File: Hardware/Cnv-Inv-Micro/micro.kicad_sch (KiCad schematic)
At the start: 48 parts, among them J1 Conn_01x03, SW1 SW_MEC_5E, U1 TMA-1205S-2WR2, U2 TMA-1205S-2WR2, U3 AMS1117-3.3, U4 STM32F103C8Tx, U5 TMA-12012S-2WR3, Y1 Crystal 8MHz

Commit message: Normalizacion placa micros
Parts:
- removed BT1: Battery_Cell, Battery:BatteryHolder_Keystone_1058_1x2032, symbol Device:Battery_Cell
- removed C15, C16: 4.7uF, Capacitor_SMD:CP_Elec_4x5.4, symbol Device:C_Polarized_Small
- removed Cnv_Control_A1: Conn_01x05, Connector_Molex:Molex_KK-254_AE-6410-05A_1x05_P2.54mm_Vertical, symbol Connector_Generic:Conn_01x05
- removed D8, D9: 1N5819WS, Diode_SMD:D_SOD-323_HandSoldering, symbol Diode:1N5819WS
- removed Inv_Pwr_A1: Conn_01x02, Connector_Molex:Molex_KK-254_AE-6410-02A_1x02_P2.54mm_Vertical, symbol Connector_Generic:Conn_01x02
- removed U5: TMA-12012S-2WR3, Converter_DCDC:Converter_DCDC_TRACO_TMA-05xxS_12xxS_Single_THT, symbol Converter_DCDC:TMA-1205S
- added Cooler, TermoSwitch: Conn_01x02, Connector_Molex:Molex_KK-254_AE-6410-02A_1x02_P2.54mm_Vertical, symbol Connector_Generic:Conn_01x02
- added Emg_Button2: Screw_Terminal_01x02, TerminalBlock_Phoenix:TerminalBlock_Phoenix_MKDS-1,5-2_1x02_P5.00mm_Horizontal, symbol Connector:Screw_Terminal_01x02
- added J3: Screw_Terminal_01x07, TerminalBlock_Phoenix:TerminalBlock_Phoenix_PT-1,5-7-5.0-H_1x07_P5.00mm_Horizontal, symbol Connector:Screw_Terminal_01x07
- added R67: 4.7k, Resistor_SMD:R_0603_1608Metric_Pad0.98x0.95mm_HandSolder, symbol Device:R
- added R68: 3.3k, Resistor_SMD:R_0603_1608Metric_Pad0.98x0.95mm_HandSolder, symbol Device:R
- added U24: PC817, Package_DIP:DIP-4_W7.62mm_SMDSocket_SmallPads, symbol Isolator:PC817
- U1: value TMA-1205S-2WR2 -> B1212S-2WR3
- U2: value TMA-1205S-2WR2 -> B1205S-2WR2
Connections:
- net 12V_Cnv: now also Cooler.1 (Pin_1)
- net 3V3_Micro: now also U24.4
- net GND_Micro: now also R68.1
- net Gnd_Cnv: now also Cooler.2 (Pin_2)
- net TermoSw_Input: now also R68.2, U24.3
- new net: TermoSwitch.2 (Pin_2), U24.1
- new net: R67.2, TermoSwitch.1 (Pin_1)
- new net 12V: R67.1
- new net Gnd_NoInsulated: U24.2
- new net Out_Emg1: Emg_Button2.2 (Pin_2)
- new net Out_Emg2: Emg_Button2.1 (Pin_1)
- new net Out_Rpm: J3.1 (Pin_1)
- new net Out_Start: J3.7 (Pin_7)
- new net Out_Stop: J3.6 (Pin_6)
- new net Out_Vel1: J3.5 (Pin_5)
- new net Out_Vel2: J3.4 (Pin_4)
- new net Out_Vel3: J3.3 (Pin_3)
- new net Out_Vel4: J3.2 (Pin_2)
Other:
- note added: "Conectores externos"
- note added: "Conectores internos"
- note added: "Es simil al del boton de emergencia"
- note added: "Es una pinera para colocar un jumper y programar directo el micro sin los 12V, si jode mucho sacalo"
- note added: "Este conector tampoco va mas, alimentacion de esp32"
- note added: "Este conector ya no va, esta en la misma placa"
- note added: "Estos manejalos como te parezca conveniente"
- note added: "Proteccion ESD"
- note added: "Y el Rele falta, pero bueno eso ya lo tenias vos"
- note added: "Yo te paso los 12V esos Y me encargo de alimentar la placa del inversor"
- moved on the sheet: C11, C12, C6, HMI_Signal_B2, Inv_Signal1_A1, Inv_Signal2_A1, J1, R10, R11, R12, R13, R14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

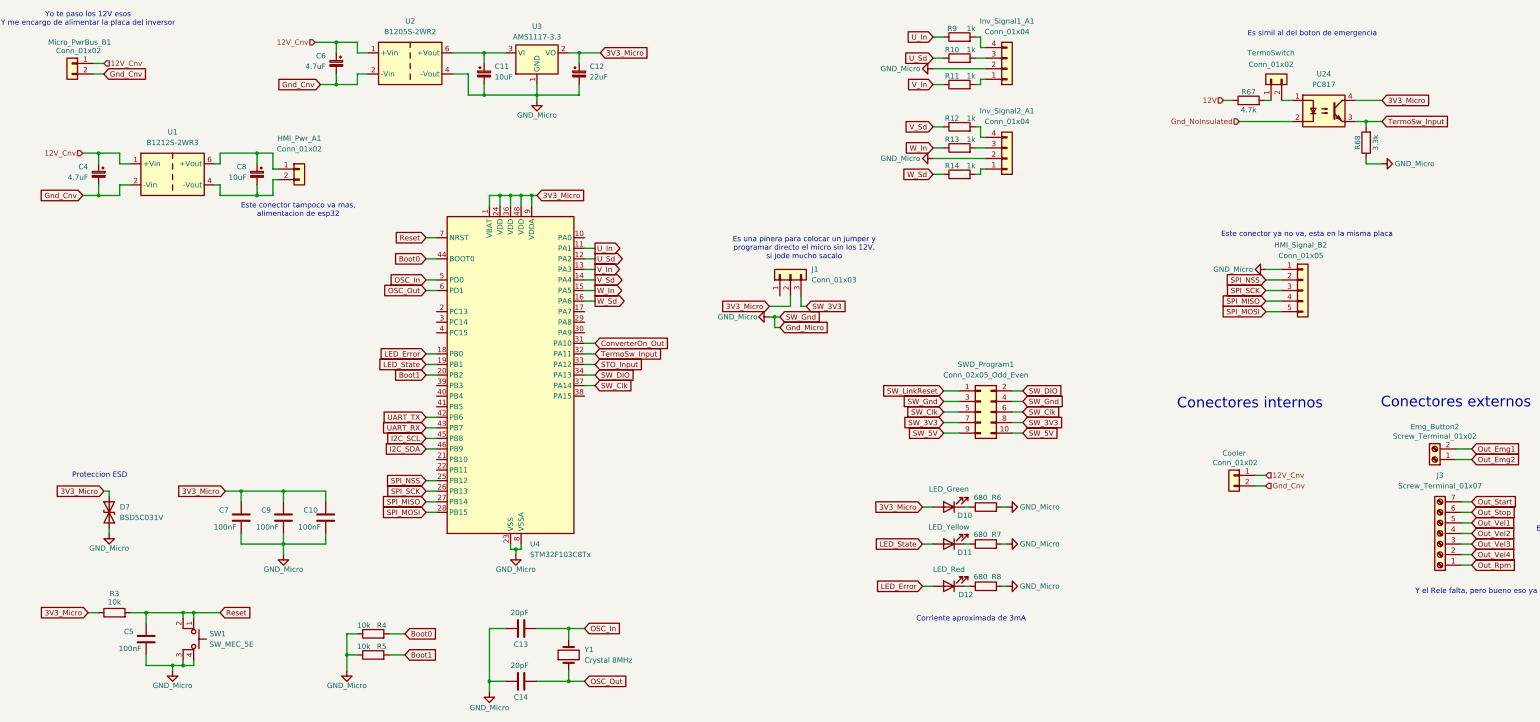
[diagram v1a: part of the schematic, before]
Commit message: Avances en PCB conversor y inversor - Simulaciones de modulacion
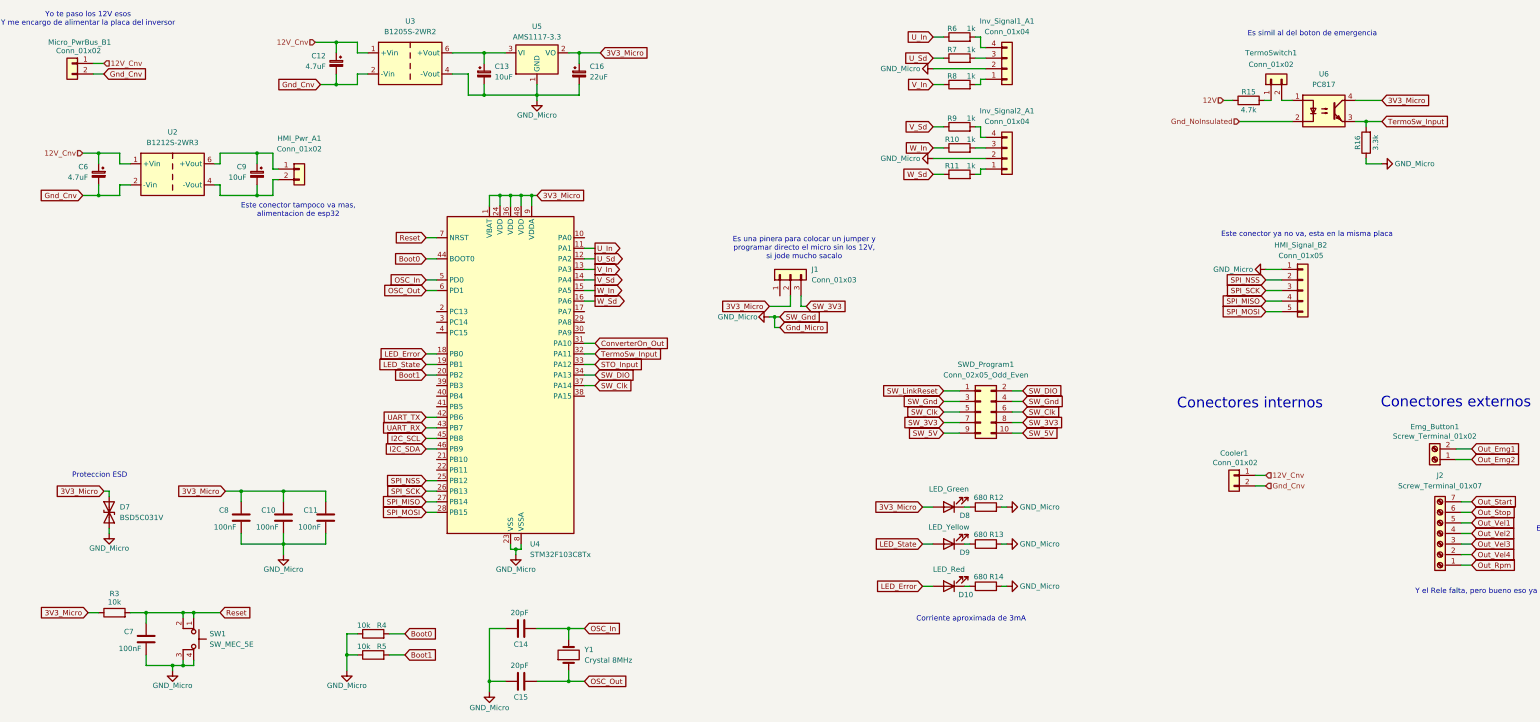
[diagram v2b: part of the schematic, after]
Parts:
- renumbered C9 to C10, C10 to C11, C6 to C12, C11 to C13, C13 to C14, C14 to C15, C12 to C16, C4 to C6, C5 to C7, C7 to C8, C8 to C9, Cooler to Cooler1, D12 to D10, D10 to D8, D11 to D9, Emg_Button2 to Emg_Button1, J3 to J2, R13 to R10, R14 to R11, R6 to R12, R7 to R13, R8 to R14, R67 to R15, R68 to R16, R9 to R6, R10 to R7, R11 to R8, R12 to R9, TermoSwitch to TermoSwitch1, U1 to U2, U2 to U3, U3 to U5, U24 to U6
